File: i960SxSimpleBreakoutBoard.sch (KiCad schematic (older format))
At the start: 26 parts, among them J1 Conn_01x07, J2 Pure Input Pins, J3 Clock, Power, and Bidirection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, J4 Conn_01x05, J5 Multiplexed Address/Data Lines, J6 Upper 16 Address Lines, U1 80960Sx

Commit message: Start to move the demux hardware onto the breakout board
Right now it is a separate module and is very annoying to wireup
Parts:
- removed J1: Conn_01x07, Connector_PinHeader_2.54mm:PinHeader_1x07_P2.54mm_Vertical, symbol Connector_Generic:Conn_01x07
- removed J2: Pure Input Pins, Connector_PinHeader_2.54mm:PinHeader_2x03_P2.54mm_Vertical, symbol Connector_Generic:Conn_02x03_Counter_Clockwise
- removed J3: Clock, Power, and Bidirectional Pins, Connector_PinHeader_2.54mm:PinHeader_2x03_P2.54mm_Vertical, symbol Connector_Generic:Conn_02x03_Counter_Clockwise
- removed J4: Conn_01x05, Connector_PinHeader_2.54mm:PinHeader_1x05_P2.54mm_Vertical, symbol Connector_Generic:Conn_01x05
- removed J5: Multiplexed Address/Data Lines, Connector_PinHeader_2.54mm:PinHeader_2x10_P2.54mm_Vertical, symbol Connector_Generic:Conn_02x10_Counter_Clockwise
- removed J6: Upper 16 Address Lines, Connector_PinHeader_2.54mm:PinHeader_2x08_P2.54mm_Vertical, symbol Connector_Generic:Conn_02x08_Counter_Clockwise
- added J?: Pure Output Pins, symbol Connector_Generic:Conn_01x08
- added J?: Interrupts, symbol Connector_Generic:Conn_01x04
- added J?: Conn_01x04, symbol Connector_Generic:Conn_01x04
- added J?: Conn_01x03, symbol Connector_Generic:Conn_01x03
- added J?: Burst Memory Lines, symbol Connector_Generic:Conn_01x04
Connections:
- wire segments 174 -> 139
- no-connect marks 2 -> 0

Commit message: Eliminate the second set of multiplexed lines all together
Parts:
- added J5: Multiplexed Address/Data Lines, Connector_PinHeader_2.54mm:PinHeader_2x10_P2.54mm_Vertical, symbol Connector_Generic:Conn_02x10_Counter_Clockwise
- added J6: Upper 16 Address Lines, Connector_PinHeader_2.54mm:PinHeader_2x08_P2.54mm_Vertical, symbol Connector_Generic:Conn_02x08_Counter_Clockwise
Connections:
- wire segments 139 -> 174
- no-connect marks 0 -> 1
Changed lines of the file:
@@
 $Descr A2 23386 16535
 encoding utf-8
-Sheet 1 2
+Sheet 1 1
 Title "i960 Partially Multiplexed Board"
 Date "2020-09-29"
@@
 	1    0    0    -1
 $EndComp
-$Sheet
-S 12150 4750 2550 1300
-U 5FD01519
-F0 "Sheet5FD01518" 50
-F1 "MultiplexedLines.sch" 50
-$EndSheet
+NoConn ~ 13950 3500
+$Comp
+L Connector_Generic:Conn_02x08_Counter_Clockwise J6
+U 1 1 5FB3656E
+P 18600 3350
+F 0 "J6" H 18650 3867 50  0000 C CNN
+F 1 "Upper 16 Address Lines" H 18650 3776 50  0000 C CNN
+F 2 "Connector_PinHeader_2.54mm:PinHeader_2x08_P2.54mm_Vertical" H 18600 3350 50  0001 C CNN
+F 3 "~" H 18600 3350 50  0001 C CNN
+	1    18600 3350
+	1    0    0    -1
+$EndComp
+$Comp
+L Connector_Generic:Conn_02x10_Counter_Clockwise J5
+U 1 1 5FAE9B72
+P 14150 3600
+F 0 "J5" H 14200 4217 50  0000 C CNN
+F 1 "Multiplexed Address/Data Lines" H 14200 4126 50  0000 C CNN
+F 2 "Connector_PinHeader_2.54mm:PinHeader_2x10_P2.54mm_Vertical" H 14150 3600 50  0001 C CNN
+F 3 "~" H 14150 3600 50  0001 C CNN
+	1    14150 3600
+	1    0    0    -1
+$EndComp
+Wire Wire Line
+	15650 3900 14450 3900
+Wire Wire Line
+	14450 3800 15650 3800
+Wire Wire Line
+	15650 3700 14450 3700
+Wire Wire Line
+	14450 3600 15650 3600
+Wire Wire Line
+	15650 3500 14450 3500
+Wire Wire Line
+	14450 3400 15650 3400
+Wire Wire Line
+	15650 3300 14450 3300
+Wire Wire Line
+	14450 3200 15650 3200
+Text Label 15650 4000 2    50   ~ 0
+AD7
+Text Label 15650 3900 0    50   ~ 0
+AD8
+Text Label 15650 3800 0    50   ~ 0
+AD9
+Text Label 15650 3700 0    50   ~ 0
+AD10
+Text Label 15650 3600 0    50   ~ 0
+AD11
+Text Label 15650 3500 0    50   ~ 0
+AD12
+Text Label 15650 3400 0    50   ~ 0
+AD13
+Text Label 15650 3300 0    50   ~ 0
+AD14
+Text Label 15650 3200 0    50   ~ 0
+AD15
+Wire Wire Line
+	14450 4000 15650 4000
+Text Label 12750 3200 0    50   ~ 0
+DT\~R
+Text Label 12750 3300 0    50   ~ 0
+~DEN
+Wire Wire Line
+	15650 4100 14450 4100
+Text Label 12750 3400 0    50   ~ 0
+ALE
+Wire Wire Line
+	13950 3400 12750 3400
+Text Label 12750 3600 2    50   ~ 0
+D0
+Wire Wire Line
+	12750 3200 13950 3200
+Text Label 15650 4100 0    50   ~ 0
+AD6
+Text Label 12750 4100 2    50   ~ 0
+AD5
+Text Label 12750 4000 2    50   ~ 0
+AD4
+Text Label 12750 3900 2    50   ~ 0
+AD3
+Text Label 12750 3800 2    50   ~ 0
+AD2
+Text Label 12750 3700 2    50   ~ 0
+AD1
+Wire Wire Line
+	13950 4100 12750 4100
+Wire Wire Line
+	12750 4000 13950 4000
+Wire Wire Line
+	13950 3900 12750 3900
+Wire Wire Line
+	12750 3800 13950 3800
+Wire Wire Line
+	13950 3700 12750 3700
+Wire Wire Line
+	12750 3600 13950 3600
+Wire Wire Line
+	13950 3300 12750 3300
+Text Label 17200 3050 0    50   ~ 0
+A16
+Text Label 17200 3150 0    50   ~ 0
+A17
+Text Label 17200 3250 0    50   ~ 0
+A18
+Text Label 17200 3350 0    50   ~ 0
+A19
+Text Label 17200 3450 0    50   ~ 0
+A20
+Text Label 17200 3550 0    50   ~ 0
+A21
+Text Label 17200 3650 0    50   ~ 0
+A22
+Text Label 17200 3750 0    50   ~ 0
+A23
+Text Label 20100 3750 2    50   ~ 0
+A24
+Text Label 20100 3650 2    50   ~ 0
+A25
+Text Label 20100 3550 2    50   ~ 0
+A26
+Text Label 20100 3450 2    50   ~ 0
+A27
+Text Label 20100 3350 2    50   ~ 0
+A28
+Text Label 20100 3250 2    50   ~ 0
+A29
+Text Label 20100 3150 2    50   ~ 0
+A30
+Text Label 20100 3050 2    50   ~ 0
+A31
+Wire Wire Line
+	18900 3050 20100 3050
+Wire Wire Line
+	20100 3150 18900 3150
+Wire Wire Line
+	18900 3250 20100 3250
+Wire Wire Line
+	20100 3350 18900 3350
+Wire Wire Line
+	18900 3450 20100 3450
+Wire Wire Line
+	20100 3550 18900 3550
+Wire Wire Line
+	18900 3650 20100 3650
+Wire Wire Line
+	20100 3750 18900 3750
+Wire Wire Line
+	18400 3750 17200 3750
+Wire Wire Line
+	17200 3650 18400 3650
+Wire Wire Line
+	17200 3050 18400 3050
+Wire Wire Line
+	18400 3150 17200 3150
+Wire Wire Line
+	17200 3250 18400 3250
+Wire Wire Line
+	18400 3350 17200 3350
+Wire Wire Line
+	17200 3450 18400 3450
+Wire Wire Line
+	18400 3550 17200 3550
 $EndSCHEMATC

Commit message: Merge demuxing components into main sheet
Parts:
- removed J5: Multiplexed Address/Data Lines, Connector_PinHeader_2.54mm:PinHeader_2x10_P2.54mm_Vertical, symbol Connector_Generic:Conn_02x10_Counter_Clockwise
- removed J6: Upper 16 Address Lines, Connector_PinHeader_2.54mm:PinHeader_2x08_P2.54mm_Vertical, symbol Connector_Generic:Conn_02x08_Counter_Clockwise
- added C? (x4): 0.1uF, Capacitor_SMD:C_0805_2012Metric_Pad1.15x1.40mm_HandSolder, symbol Device:C
- added U? (x2): 74HC573, Package_DIP:DIP-20_W7.62mm_Socket, symbol 74xx:74LS573
- added U? (x2): 74HC245, Package_DIP:DIP-20_W7.62mm_Socket, symbol 74xx:74HC245
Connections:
- net labels added: A0, A1, A10, A11, A12, A13, A14, A15, A2, A3, A4, A5, A6, A7, A8, A9, D0', D1, D10, D11, D12, D13, D14, D15, D2, D3, D4, D5, D6, D7, D8, D9
- wire segments 174 -> 246
- no-connect marks 1 -> 0

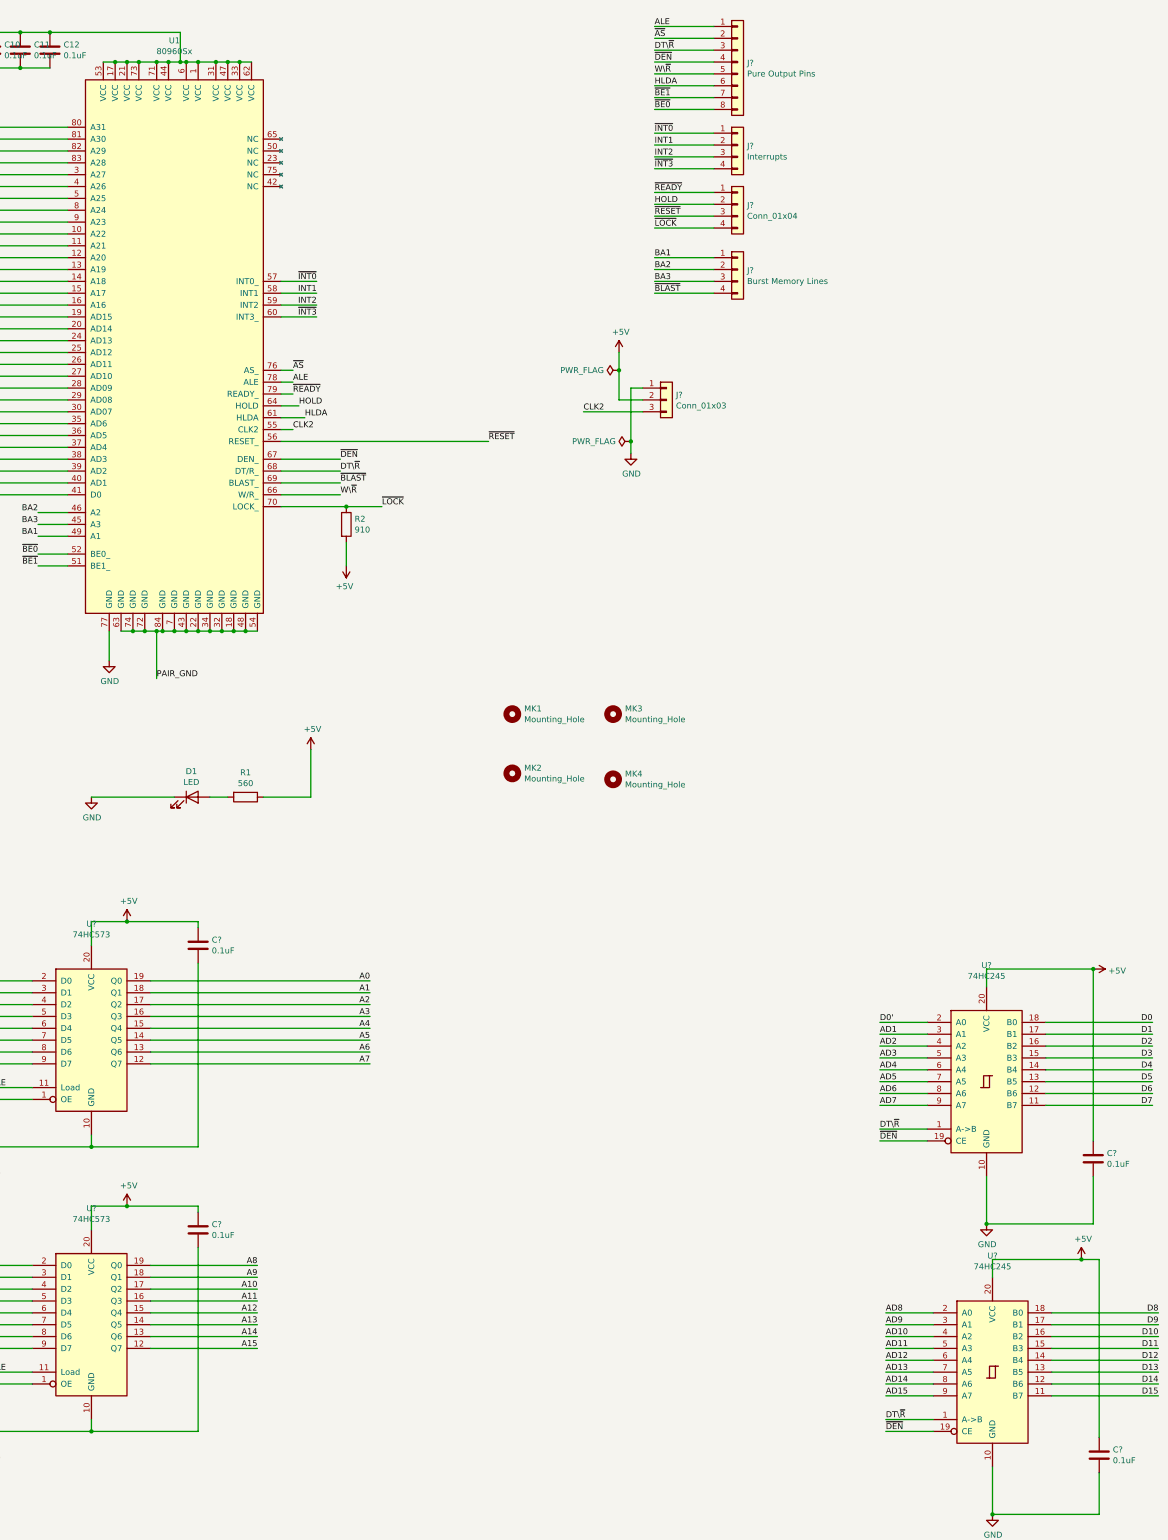
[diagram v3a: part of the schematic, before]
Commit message: Consolidate control lines into fewer headers
Address lines now have a single 01x32 header
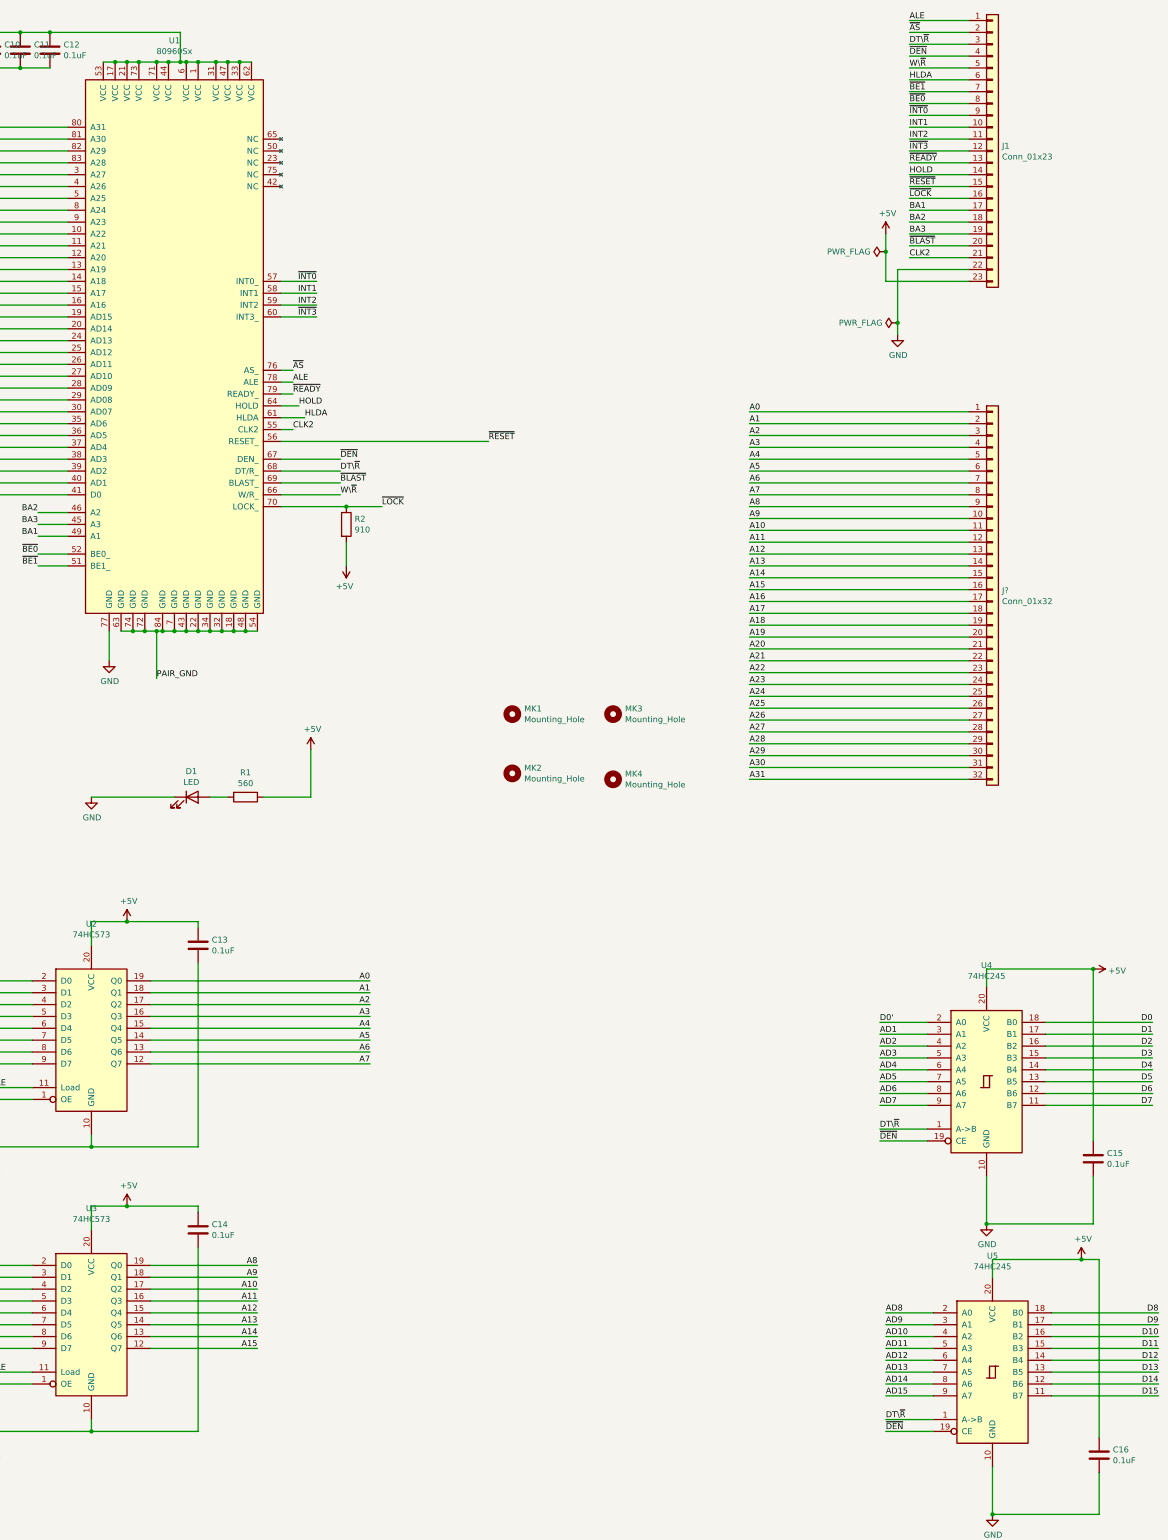
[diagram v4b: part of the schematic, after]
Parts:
- removed J?: Pure Output Pins, symbol Connector_Generic:Conn_01x08
- removed J?: Interrupts, symbol Connector_Generic:Conn_01x04
- removed J?: Conn_01x04, symbol Connector_Generic:Conn_01x04
- removed J?: Conn_01x03, symbol Connector_Generic:Conn_01x03
- removed J?: Burst Memory Lines, symbol Connector_Generic:Conn_01x04
- added J1: Conn_01x23, symbol Connector_Generic:Conn_01x23
- added J?: Conn_01x32, symbol Connector_Generic:Conn_01x32
- gave numbers to parts that had none: 8
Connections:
- net +5V: now also J1.23 (Pin_23)
- net A0: now also J?.1 (Pin_1)
- net A1: now also J?.2 (Pin_2)
- net A10: now also J?.11 (Pin_11)
- net A11: now also J?.12 (Pin_12)
- net A12: now also J?.13 (Pin_13)
- net A13: now also J?.14 (Pin_14)
- net A14: now also J?.15 (Pin_15)
- net A15: now also J?.16 (Pin_16)
- net A16: now also J?.17 (Pin_17)
- net A17: now also J?.18 (Pin_18)
- net A18: now also J?.19 (Pin_19)
- net A19: now also J?.20 (Pin_20)
- net A2: now also J?.3 (Pin_3)
- net A20: now also J?.21 (Pin_21)
- net A21: now also J?.22 (Pin_22)
- net A22: now also J?.23 (Pin_23)
- net A23: now also J?.24 (Pin_24)
- net A24: now also J?.25 (Pin_25)
- net A25: now also J?.26 (Pin_26)
- net A26: now also J?.27 (Pin_27)
- net A27: now also J?.28 (Pin_28)
- net A28: now also J?.29 (Pin_29)
- net A29: now also J?.30 (Pin_30)
- net A3: now also J?.4 (Pin_4)
- net A30: now also J?.31 (Pin_31)
- net A31: now also J?.32 (Pin_32)
- net A4: now also J?.5 (Pin_5)
- net A5: now also J?.6 (Pin_6)
- net A6: now also J?.7 (Pin_7)
- net A7: now also J?.8 (Pin_8)
- net A8: now also J?.9 (Pin_9)
- net A9: now also J?.10 (Pin_10)
- net ALE: now also J1.1 (Pin_1)
- net BA1: now also J1.17 (Pin_17)
- net BA2: now also J1.18 (Pin_18)
- net BA3: now also J1.19 (Pin_19)
- net CLK2: now also J1.21 (Pin_21)
- net DT\~R: now also J1.3 (Pin_3)
- net GND: now also J1.22 (Pin_22)
- net HLDA: now also J1.6 (Pin_6)
- net HOLD: now also J1.14 (Pin_14)
- net INT1: now also J1.10 (Pin_10)
- net INT2: now also J1.11 (Pin_11)
- net W\~R: now also J1.5 (Pin_5)
- net ~AS: now also J1.2 (Pin_2)
- net ~BE0: now also J1.8 (Pin_8)
- net ~BE1: now also J1.7 (Pin_7)
- net ~BLAST: now also J1.20 (Pin_20)
- net ~DEN: now also J1.4 (Pin_4)
- net ~INT0: now also J1.9 (Pin_9)
- net ~INT3: now also J1.12 (Pin_12)
- net ~LOCK: now also J1.16 (Pin_16)
- net ~READY: now also J1.13 (Pin_13)
- net ~RESET: now also J1.15 (Pin_15)

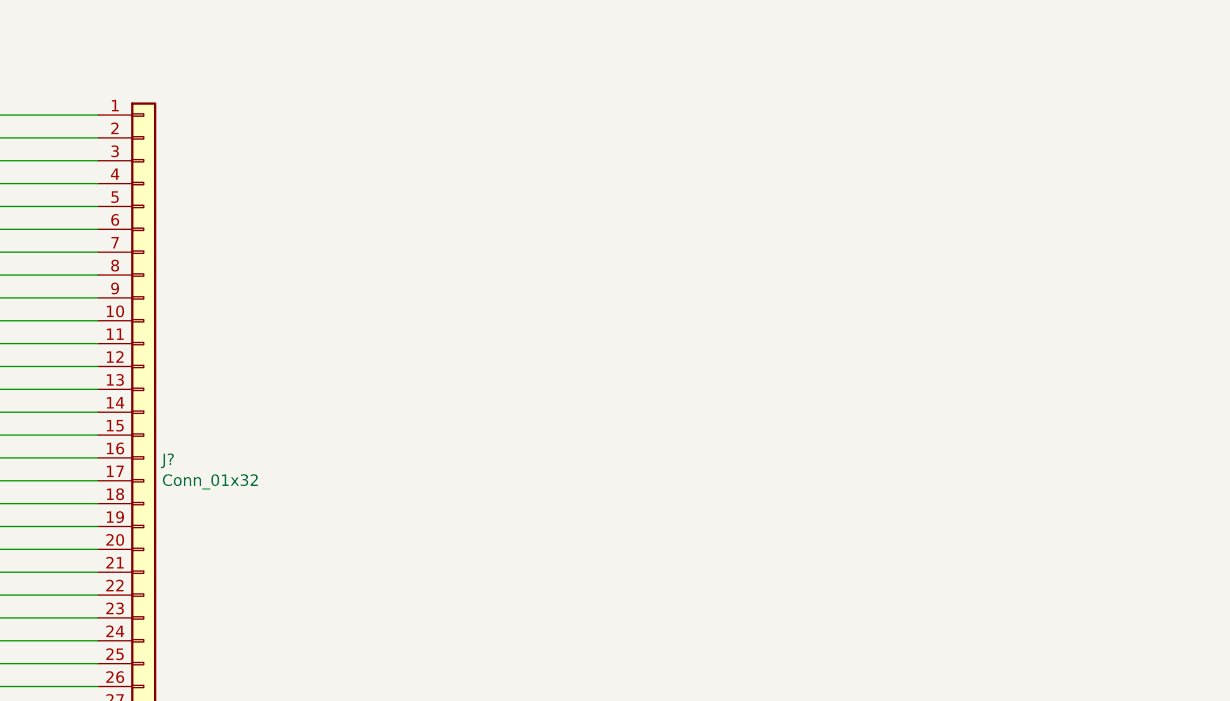
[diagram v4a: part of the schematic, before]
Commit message: Add the data line breakout
No sanity check errors :)
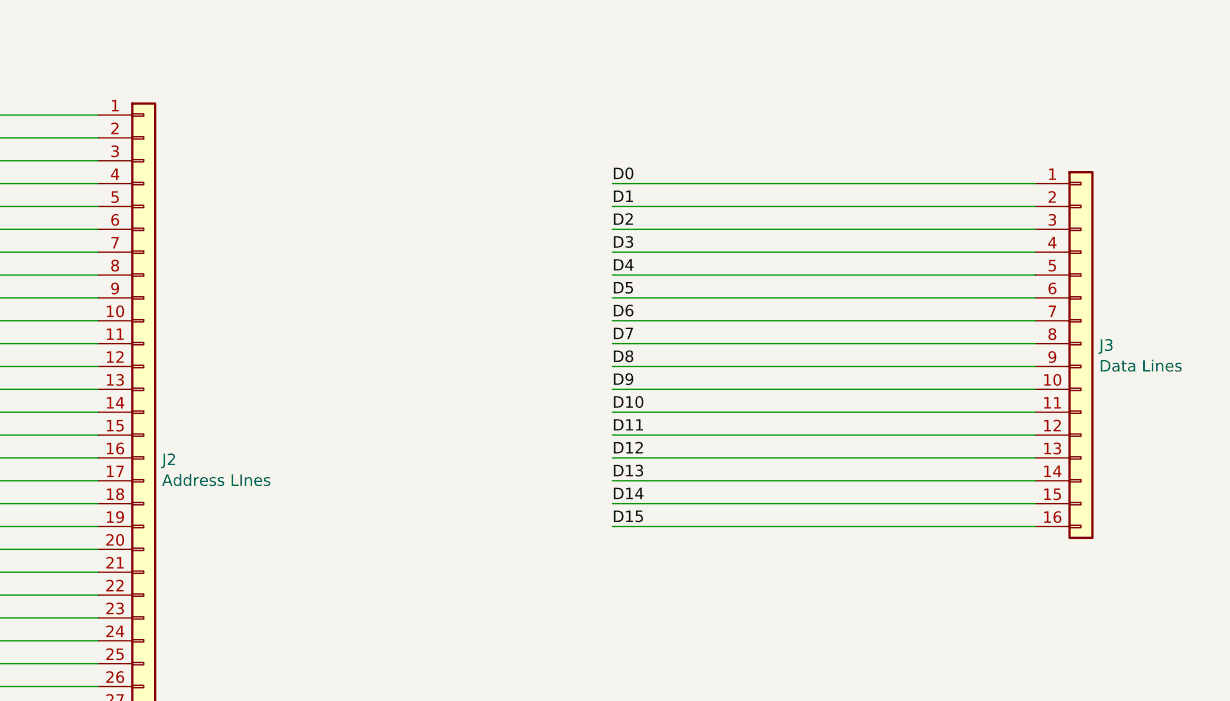
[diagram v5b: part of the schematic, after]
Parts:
- added J3: Data Lines, symbol Connector_Generic:Conn_01x16
- J2: renamed from J?; value Conn_01x32 -> Address LInes
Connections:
- net D0: now also J3.1 (Pin_1)
- net D1: now also J3.2 (Pin_2)
- net D10: now also J3.11 (Pin_11)
- net D11: now also J3.12 (Pin_12)
- net D12: now also J3.13 (Pin_13)
- net D13: now also J3.14 (Pin_14)
- net D14: now also J3.15 (Pin_15)
- net D15: now also J3.16 (Pin_16)
- net D2: now also J3.3 (Pin_3)
- net D3: now also J3.4 (Pin_4)
- net D4: now also J3.5 (Pin_5)
- net D5: now also J3.6 (Pin_6)
- net D6: now also J3.7 (Pin_7)
- net D7: now also J3.8 (Pin_8)
- net D8: now also J3.9 (Pin_9)
- net D9: now also J3.10 (Pin_10)
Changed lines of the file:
@@
 	11550 3150 12250 3150
 $Comp
-L Connector_Generic:Conn_01x32 J?
+L Connector_Generic:Conn_01x32 J2
 U 1 1 606DD184
 P 12450 5750
-F 0 "J?" H 12530 5742 50  0000 L CNN
-F 1 "Conn_01x32" H 12530 5651 50  0000 L CNN
+F 0 "J2" H 12530 5742 50  0000 L CNN
+F 1 "Address LInes" H 12530 5651 50  0000 L CNN
 F 2 "" H 12450 5750 50  0001 C CNN
 F 3 "~" H 12450 5750 50  0001 C CNN
@@
 Text Label 10400 7350 0    50   ~ 0
 A31
+$Comp
+L Connector_Generic:Conn_01x16 J3
+U 1 1 609DCE40
+P 16550 5250
+F 0 "J3" H 16630 5242 50  0000 L CNN
+F 1 "Data Lines" H 16630 5151 50  0000 L CNN
+F 2 "" H 16550 5250 50  0001 C CNN
+F 3 "~" H 16550 5250 50  0001 C CNN
+	1    16550 5250
+	1    0    0    -1
+$EndComp
+Wire Wire Line
+	16350 4650 14500 4650
+Wire Wire Line
+	16350 4750 14500 4750
+Wire Wire Line
+	16350 4850 14500 4850
+Wire Wire Line
+	16350 4950 14500 4950
+Wire Wire Line
+	16350 5050 14500 5050
+Wire Wire Line
+	16350 5150 14500 5150
+Wire Wire Line
+	16350 5250 14500 5250
+Wire Wire Line
+	16350 4550 14500 4550
+Wire Wire Line
+	14500 5350 16350 5350
+Wire Wire Line
+	14500 5450 16350 5450
+Wire Wire Line
+	14500 5550 16350 5550
+Wire Wire Line
+	14500 5650 16350 5650
+Wire Wire Line
+	14500 5750 16350 5750
+Wire Wire Line
+	14500 5850 16350 5850
+Wire Wire Line
+	14500 5950 16350 5950
+Wire Wire Line
+	14500 6050 16350 6050
+Text Label 14500 4550 0    50   ~ 0
+D0
+Text Label 14500 4650 0    50   ~ 0
+D1
+Text Label 14500 4750 0    50   ~ 0
+D2
+Text Label 14500 4850 0    50   ~ 0
+D3
+Text Label 14500 4950 0    50   ~ 0
+D4
+Text Label 14500 5050 0    50   ~ 0
+D5
+Text Label 14500 5150 0    50   ~ 0
+D6
+Text Label 14500 5250 0    50   ~ 0
+D7
+Text Label 14500 5350 0    50   ~ 0
+D8
+Text Label 14500 5450 0    50   ~ 0
+D9
+Text Label 14500 5550 0    50   ~ 0
+D10
+Text Label 14500 5650 0    50   ~ 0
+D11
+Text Label 14500 5750 0    50   ~ 0
+D12
+Text Label 14500 5850 0    50   ~ 0
+D13
+Text Label 14500 5950 0    50   ~ 0
+D14
+Text Label 14500 6050 0    50   ~ 0
+D15
 $EndSCHEMATC
